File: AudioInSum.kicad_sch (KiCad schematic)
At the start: 18 parts, among them U7 TLV9062IDR

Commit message: Moved everything to the top side
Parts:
- C5: footprint Capacitor_SMD:C_0402_1005Metric -> Capacitor_SMD:C_0603_1608Metric
- R10, R18, R19, R24, R25, R7, R8, R9: footprint Resistor_SMD:R_0402_1005Metric -> Resistor_SMD:R_0603_1608Metric
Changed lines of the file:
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@@
       (effects (font (size 1.27 1.27)) (justify left))
     )
-    (property "Footprint" "Resistor_SMD:R_0402_1005Metric" (at 108.966 61.214 90)
+    (property "Footprint" "Resistor_SMD:R_0603_1608Metric" (at 108.966 61.214 90)
       (effects (font (size 1.27 1.27)) hide)
     )
@@
       (effects (font (size 1.27 1.27)) (justify left))
     )
-    (property "Footprint" "Capacitor_SMD:C_0402_1005Metric" (at 144.4752 167.64 0)
+    (property "Footprint" "Capacitor_SMD:C_0603_1608Metric" (at 144.4752 167.64 0)
       (effects (font (size 1.27 1.27)) hide)
     )
@@
       (effects (font (size 1.27 1.27)))
     )
-    (property "Footprint" "Resistor_SMD:R_0402_1005Metric" (at 178.181 108.966 90)
+    (property "Footprint" "Resistor_SMD:R_0603_1608Metric" (at 178.181 108.966 90)
       (effects (font (size 1.27 1.27)) hide)
     )
@@
       (effects (font (size 1.27 1.27)))
     )
-    (property "Footprint" "Resistor_SMD:R_0402_1005Metric" (at 158.496 64.516 90)
+    (property "Footprint" "Resistor_SMD:R_0603_1608Metric" (at 158.496 64.516 90)
       (effects (font (size 1.27 1.27)) hide)
     )
@@
       (effects (font (size 1.27 1.27)) (justify left))
     )
-    (property "Footprint" "Resistor_SMD:R_0402_1005Metric" (at 129.921 109.474 90)
+    (property "Footprint" "Resistor_SMD:R_0603_1608Metric" (at 129.921 109.474 90)
       (effects (font (size 1.27 1.27)) hide)
     )
@@
       (effects (font (size 1.27 1.27)) (justify left))
     )
-    (property "Footprint" "Resistor_SMD:R_0402_1005Metric" (at 131.191 96.774 90)
+    (property "Footprint" "Resistor_SMD:R_0603_1608Metric" (at 131.191 96.774 90)
       (effects (font (size 1.27 1.27)) hide)
     )
@@
       (effects (font (size 1.27 1.27)) (justify left))
     )
-    (property "Footprint" "Resistor_SMD:R_0402_1005Metric" (at 115.316 109.474 90)
+    (property "Footprint" "Resistor_SMD:R_0603_1608Metric" (at 115.316 109.474 90)
       (effects (font (size 1.27 1.27)) hide)
     )
@@
       (effects (font (size 1.27 1.27)) (justify left))
     )
-    (property "Footprint" "Resistor_SMD:R_0402_1005Metric" (at 132.461 47.879 90)
+    (property "Footprint" "Resistor_SMD:R_0603_1608Metric" (at 132.461 47.879 90)
       (effects (font (size 1.27 1.27)) hide)
     )
@@
       (effects (font (size 1.27 1.27)))
     )
-    (property "Footprint" "Resistor_SMD:R_0402_1005Metric" (at 185.674 49.276 90)
+    (property "Footprint" "Resistor_SMD:R_0603_1608Metric" (at 185.674 49.276 90)
       (effects (font (size 1.27 1.27)) hide)
     )
@@
       (effects (font (size 1.27 1.27)))
     )
-    (property "Footprint" "Resistor_SMD:R_0402_1005Metric" (at 158.496 119.126 90)
+    (property "Footprint" "Resistor_SMD:R_0603_1608Metric" (at 158.496 119.126 90)
       (effects (font (size 1.27 1.27)) hide)
     )
@@
       (effects (font (size 1.27 1.27)))
     )
-    (property "Footprint" "Resistor_SMD:R_0402_1005Metric" (at 185.674 101.346 90)
+    (property "Footprint" "Resistor_SMD:R_0603_1608Metric" (at 185.674 101.346 90)
       (effects (font (size 1.27 1.27)) hide)
     )
@@
       (effects (font (size 1.27 1.27)))
     )
-    (property "Footprint" "Resistor_SMD:R_0402_1005Metric" (at 178.816 56.896 90)
+    (property "Footprint" "Resistor_SMD:R_0603_1608Metric" (at 178.816 56.896 90)
       (effects (font (size 1.27 1.27)) hide)
     )
@@
       (effects (font (size 1.27 1.27)))
     )
-    (property "Footprint" "Resistor_SMD:R_0402_1005Metric" (at 149.606 70.104 90)
+    (property "Footprint" "Resistor_SMD:R_0603_1608Metric" (at 149.606 70.104 90)
       (effects (font (size 1.27 1.27)) hide)
     )
@@
       (effects (font (size 1.27 1.27)))
     )
-    (property "Footprint" "Resistor_SMD:R_0402_1005Metric" (at 149.606 123.444 90)
+    (property "Footprint" "Resistor_SMD:R_0603_1608Metric" (at 149.606 123.444 90)
       (effects (font (size 1.27 1.27)) hide)
     )
@@
       (effects (font (size 1.27 1.27)) (justify left))
     )
-    (property "Footprint" "Resistor_SMD:R_0402_1005Metric" (at 132.334 60.706 90)
-      (effects (font (size 1.27 1.27)) hide)
-    )
+    (property "Footprint" "Resistor_SMD:R_0603_1608Metric" (at 132.334 60.706 90)
+      (effects (font (size 1.27 1.27)) hide)
+    )

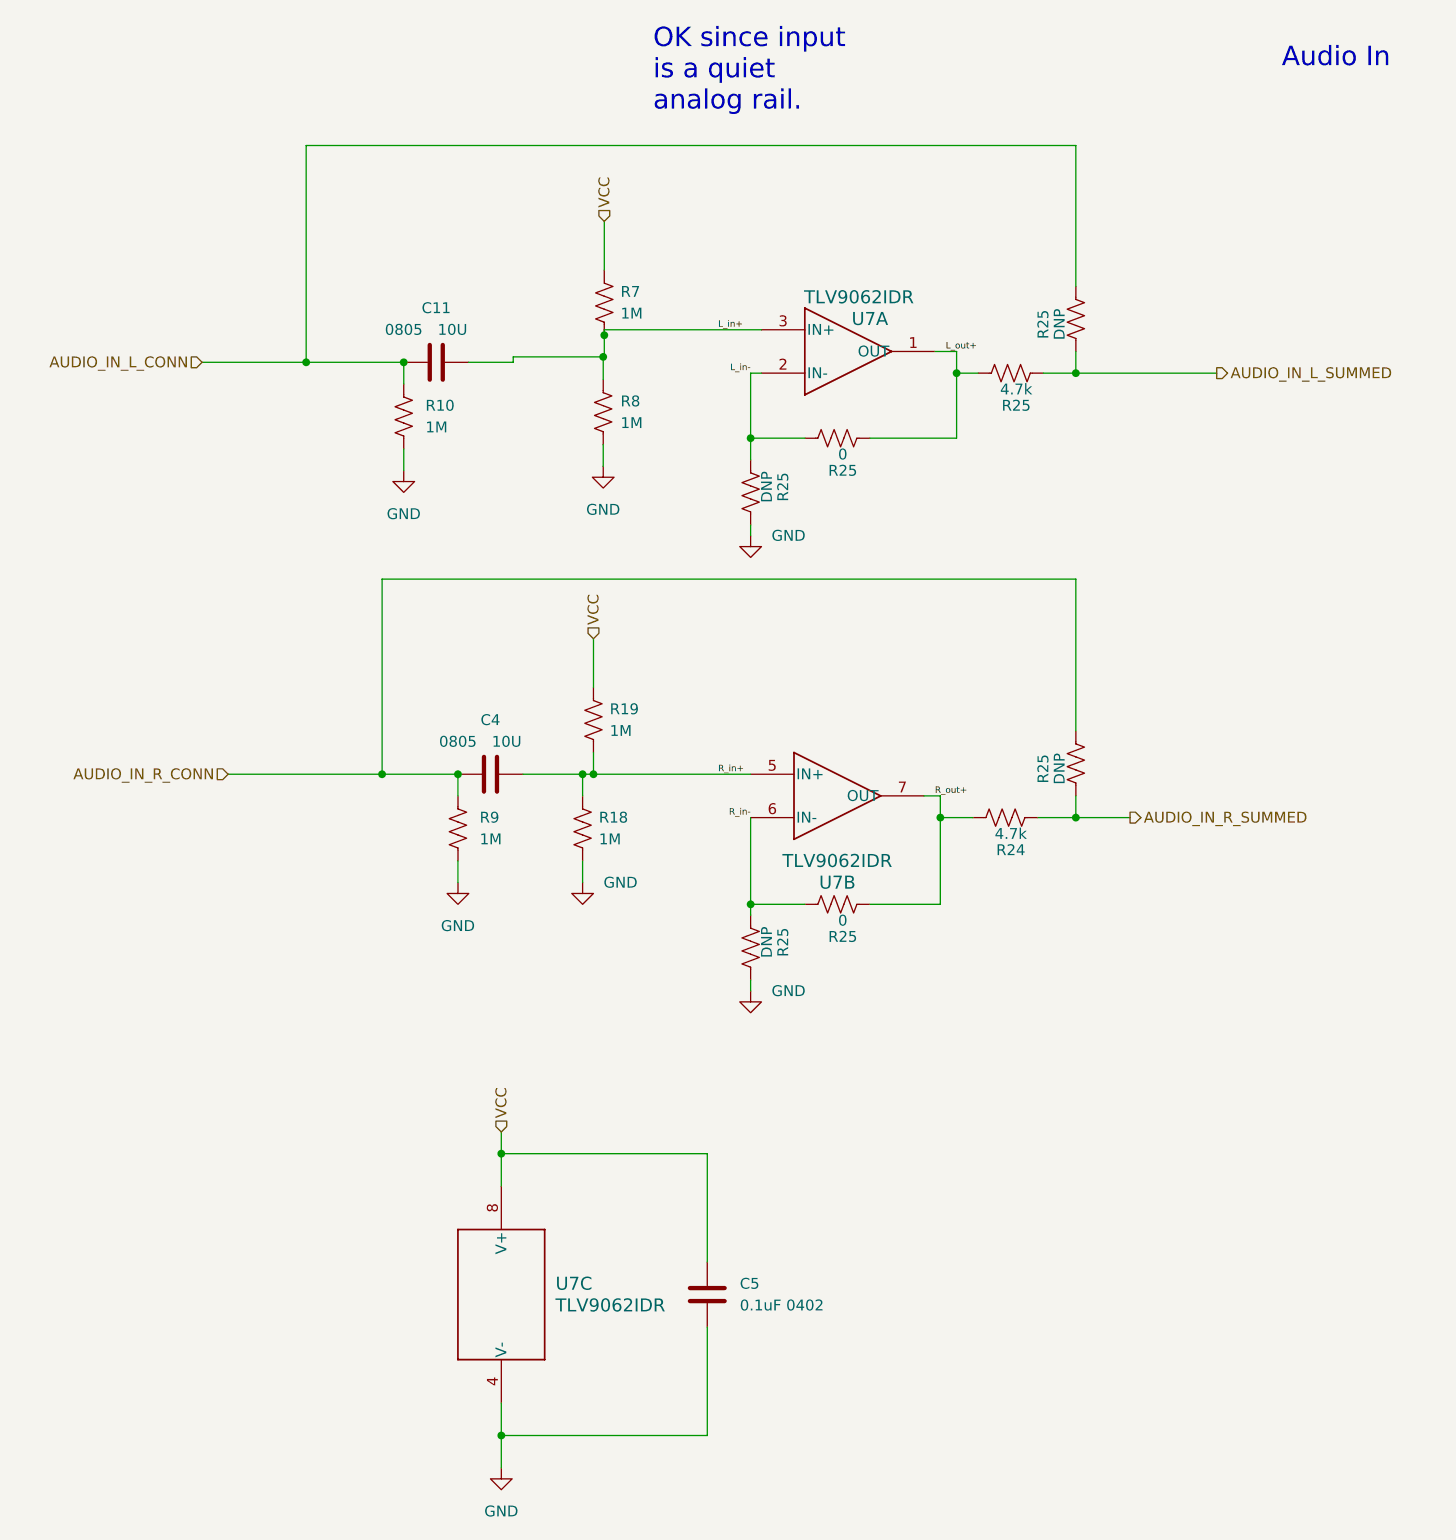
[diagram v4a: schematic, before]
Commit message: adding script to pull prices and availability from Mouser
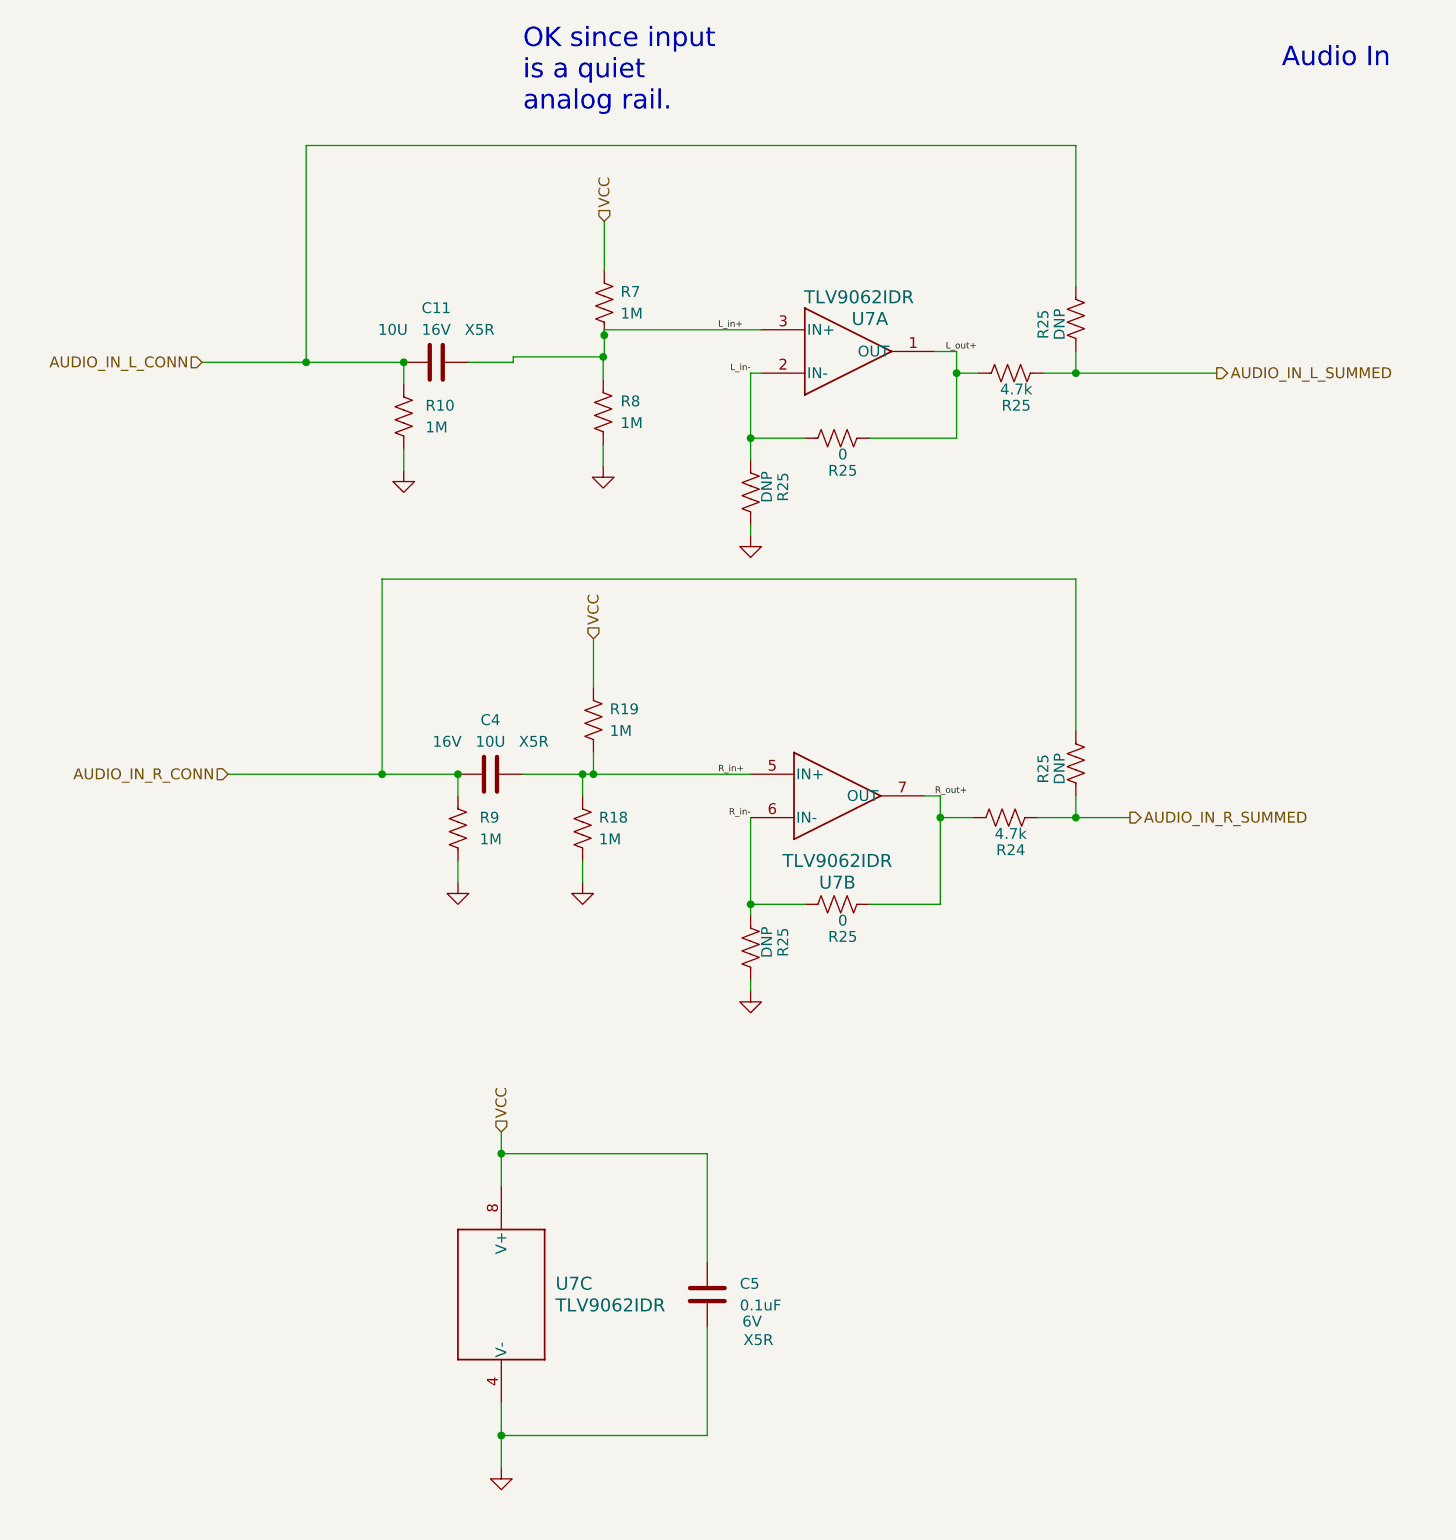
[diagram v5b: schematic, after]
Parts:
- C11, C4: Specs 0805 -> (none); Type (none) -> X5R; Voltage (none) -> 16V
- C5: value 0.1uF 0402 -> 0.1uF; Type (none) -> X5R; Voltage (none) -> 6V
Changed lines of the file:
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@@
     (effects (font (size 2.27 2.27)) (justify left bottom))
   )
-  (text "OK since input\nis a quiet\nanalog rail." (at 137.16 25.4 0)
+  (text "OK since input\nis a quiet\nanalog rail." (at 121.92 25.4 0)
     (effects (font (size 2.27 2.27)) (justify left bottom))
   )
@@
   )
   (symbol (lib_id "Device:C") (at 143.51 163.83 0) (unit 1)
-    (in_bom yes) (on_board yes) (dnp no) (fields_autoplaced)
+    (in_bom yes) (on_board yes) (dnp no)
     (property "Reference" "C5" (at 147.32 162.56 0)
       (effects (font (size 1.27 1.27)) (justify left))
     )
-    (property "Value" "0.1uF 0402" (at 147.32 165.1 0)
+    (property "Value" "0.1uF" (at 147.32 165.1 0)
       (effects (font (size 1.27 1.27)) (justify left))
     )
@@
       (effects (font (size 1.27 1.27)) hide)
     )
+    (property "Voltage" "6V" (at 148.7594 166.9868 0)
+      (effects (font (size 1.27 1.27)))
+    )
+    (property "Type" "X5R" (at 149.501 169.1479 0)
+      (effects (font (size 1.27 1.27)))
+    )
     (pin "1")
     (pin "2")
@@
     )
     (property "Value" "GND" (at 119.38 189.23 0)
-      (effects (font (size 1.27 1.27)))
+      (effects (font (size 1.27 1.27)) hide)
     )
     (property "Footprint" "" (at 119.38 184.15 0)
@@
     )
     (property "Value" "GND" (at 131.318 71.882 0)
-      (effects (font (size 1.27 1.27)))
+      (effects (font (size 1.27 1.27)) hide)
     )
     (property "Footprint" "" (at 131.318 66.802 0)
@@
     )
     (property "Value" "GND" (at 107.95 72.39 0)
-      (effects (font (size 1.27 1.27)))
+      (effects (font (size 1.27 1.27)) hide)
     )
     (property "Footprint" "" (at 107.95 67.31 0)
@@
       (effects (font (size 1.27 1.27)))
     )
-    (property "Value" "10U" (at 113.665 50.8 90)
+    (property "Value" "10U" (at 106.68 50.8 90)
       (effects (font (size 1.27 1.27)))
     )
@@
       (effects (font (size 1.27 1.27)) hide)
     )
-    (property "Specs" "0805" (at 107.95 50.8 90)
+    (property "Voltage" "16V" (at 111.76 50.8 90)
+      (effects (font (size 1.27 1.27)))
+    )
+    (property "Type" "X5R" (at 116.84 50.8 90)
       (effects (font (size 1.27 1.27)))
     )
@@
     )
     (property "Value" "GND" (at 133.35 115.57 0)
-      (effects (font (size 1.27 1.27)))
+      (effects (font (size 1.27 1.27)) hide)
     )
     (property "Footprint" "" (at 128.905 115.57 0)
@@
       (effects (font (size 1.27 1.27)))
     )
-    (property "Value" "10U" (at 120.015 99.06 90)
+    (property "Value" "10U" (at 118.11 99.06 90)
       (effects (font (size 1.27 1.27)))
     )
@@
       (effects (font (size 1.27 1.27)) hide)
     )
-    (property "Specs" "0805" (at 114.3 99.06 90)
+    (property "Voltage" "16V" (at 113.03 99.06 90)
+      (effects (font (size 1.27 1.27)))
+    )
+    (property "Type" "X5R" (at 123.19 99.06 90)
       (effects (font (size 1.27 1.27)))
     )
@@
     )
     (property "Value" "GND" (at 114.3 120.65 0)
-      (effects (font (size 1.27 1.27)))
+      (effects (font (size 1.27 1.27)) hide)
     )
     (property "Footprint" "" (at 114.3 115.57 0)
@@
     )
     (property "Value" "GND" (at 153.035 128.27 0)
-      (effects (font (size 1.27 1.27)))
+      (effects (font (size 1.27 1.27)) hide)
     )
     (property "Footprint" "" (at 148.59 128.27 0)
@@
     )
     (property "Value" "GND" (at 153.035 74.93 0)
-      (effects (font (size 1.27 1.27)))
+      (effects (font (size 1.27 1.27)) hide)
     )
     (property "Footprint" "" (at 148.59 74.93 0)

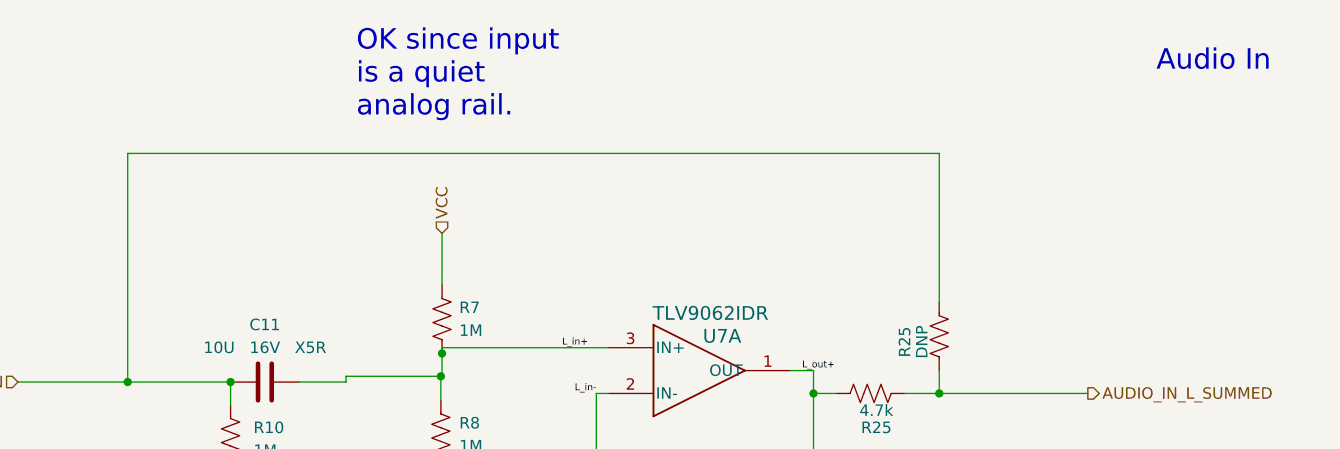
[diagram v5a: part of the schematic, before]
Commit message: script working to generate Mouser, Digikey, and JLPCB BOMS
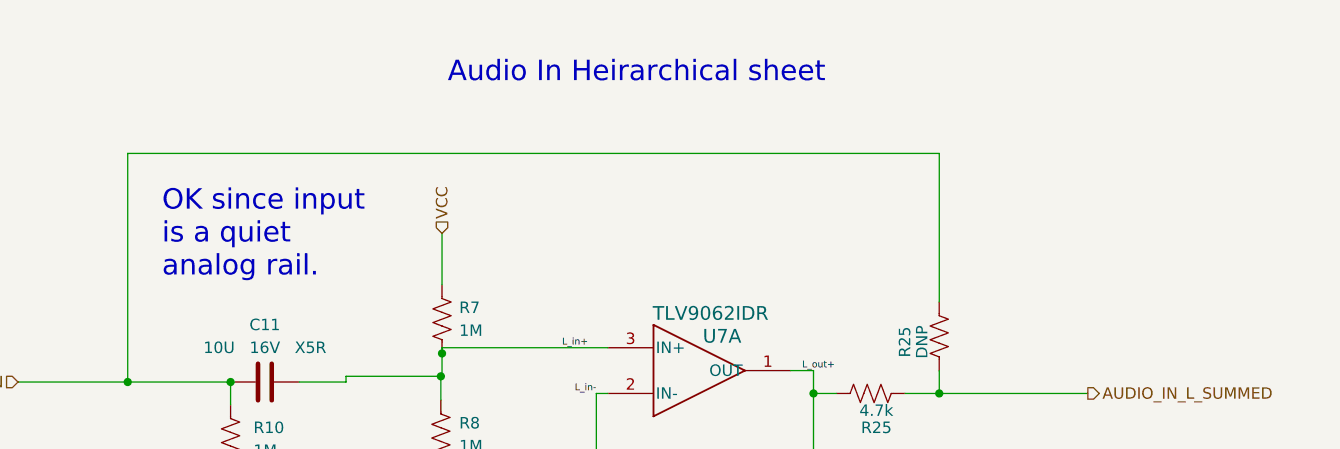
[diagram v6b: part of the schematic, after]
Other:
- note added: "Audio In Heirarchical sheet"
- note removed: "Audio In"
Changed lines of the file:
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@@
     (stroke (width 0) (type default))
   )
-  (text "Audio In" (at 210.82 20.32 0)
+  (text "Audio In Heirarchical sheet" (at 132.08 21.59 0)
     (effects (font (size 2.27 2.27)) (justify left bottom))
   )
-  (text "OK since input\nis a quiet\nanalog rail." (at 121.92 25.4 0)
+  (text "OK since input\nis a quiet\nanalog rail." (at 100.33 43.18 0)
     (effects (font (size 2.27 2.27)) (justify left bottom))
   )
